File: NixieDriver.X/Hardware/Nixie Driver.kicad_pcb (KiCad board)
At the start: 4 copper layers, 21.1 x 31.8 mm, 20 parts, among them J1 Conn_02x03_Odd_Even, J2 Conn_01x03, J3 Conn_02x03_Odd_Even, Q0 MMBTA42LT1G, Q1 MMBTA42LT1G, Q10 MMBTA42LT1G, Q2 MMBTA42LT1G, Q3 MMBTA42LT1G, Q4 MMBTA42LT1G, Q5 MMBTA42LT1G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

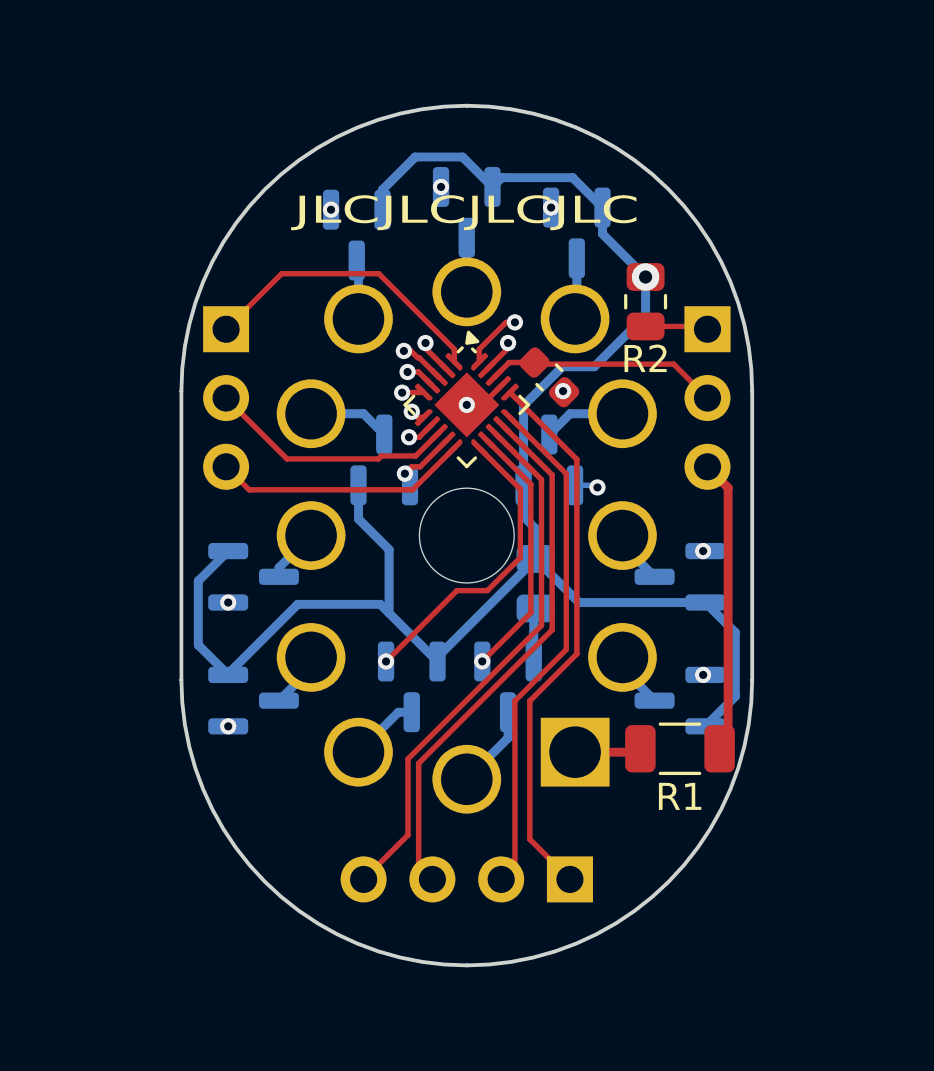
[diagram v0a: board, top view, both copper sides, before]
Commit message: Current-limiting-resistor for each driver
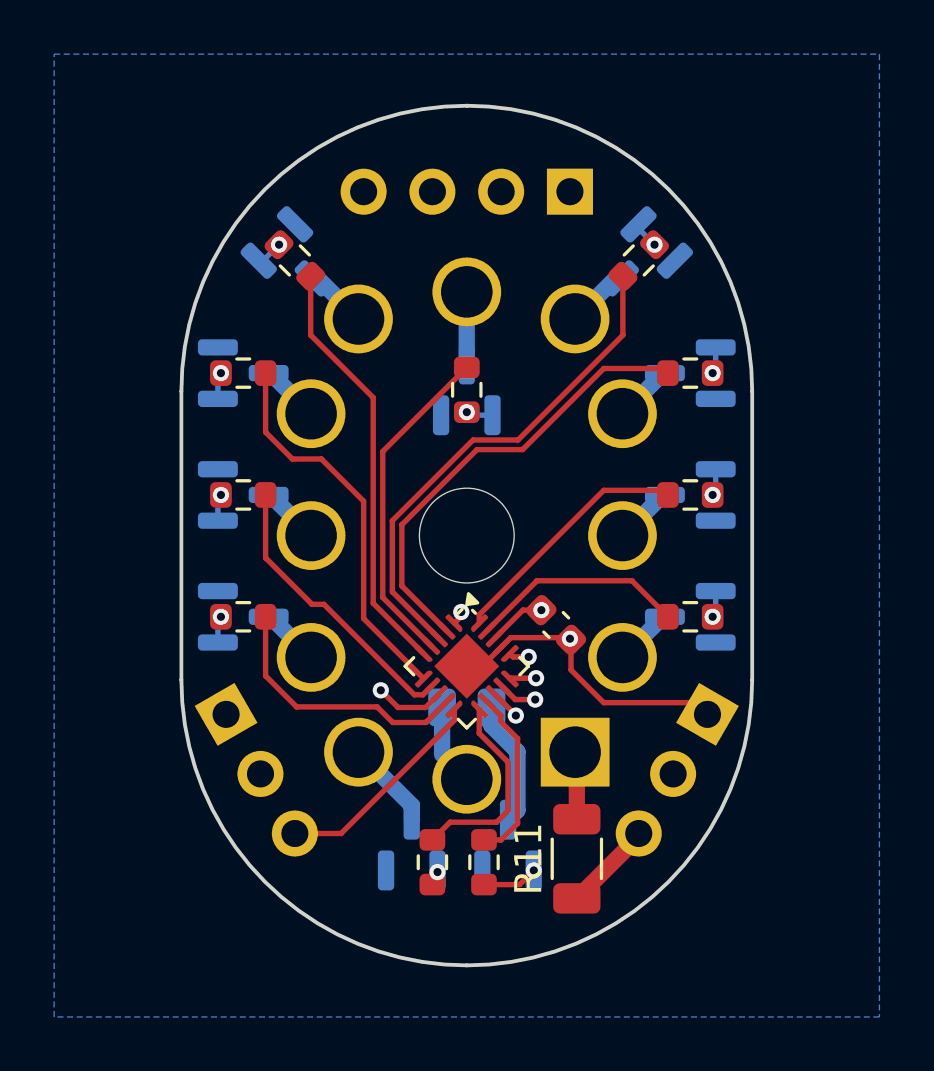
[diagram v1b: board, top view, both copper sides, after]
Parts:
- added R0: 2.2k, Resistor_SMD:R_0603_1608Metric, F.Cu at (160.7, 104.6)
- added R10: 2.2k, Resistor_SMD:R_0603_1608Metric, F.Cu at (153.0, 113.7)
- added R11: 20k, Resistor_SMD:R_1206_3216Metric, F.Cu at (156.5, 113.5)
- added R12: 150k, Resistor_SMD:R_0805_2012Metric, B.Cu at (152.4, 108.0)
- added R4: 2.2k, Resistor_SMD:R_0603_1608Metric, F.Cu at (144.1, 95.6)
- added R5: 2.2k, Resistor_SMD:R_0603_1608Metric, F.Cu at (146.1, 91.4)
- added R6: 2.2k, Resistor_SMD:R_0603_1608Metric, F.Cu at (152.4, 96.2)
- added R7: 2.2k, Resistor_SMD:R_0603_1608Metric, F.Cu at (158.8, 91.4)
- added R8: 2.2k, Resistor_SMD:R_0603_1608Metric, F.Cu at (160.7, 95.6)
- added R9: 2.2k, Resistor_SMD:R_0603_1608Metric, F.Cu at (160.7, 100.1)
- R1: value 20k -> 2.2k; footprint Resistor_SMD:R_1206_3216Metric -> Resistor_SMD:R_0603_1608Metric
- R2: footprint Resistor_SMD:R_0805_2012Metric -> Resistor_SMD:R_0603_1608Metric
- R3: value 0 -> 2.2k; footprint Resistor_SMD:R_0805_2012Metric -> Resistor_SMD:R_0603_1608Metric; moved to F.Cu
- moved J2 25.4 mm to (156.2, 88.9)
- moved R2 18.9 mm to (144.1, 104.6), turned to 180 degrees
- moved J1 14.2 mm to (143.5, 108.2), turned to -150 degrees
- moved J3 14.2 mm to (161.3, 108.2), turned to 150 degrees
- moved R3 11.3 mm to (144.1, 100.1), turned to 180 degrees
- moved R1 10.1 mm to (151.1, 113.7), turned to -90 degrees
- moved U1 9.65 mm to (152.4, 106.4)
- moved C1 9.15 mm to (155.7, 104.9)
- moved Q6 6.56 mm to (152.4, 96.2), turned to 90.029 degrees
- moved Q4 6.11 mm to (144.1, 95.6), turned to 0 degrees
- moved Q8 6.11 mm to (160.7, 95.6), turned to 180 degrees
- moved Q1 5.84 mm to (150.4, 113.0), turned to 90 degrees
- moved Q10 5.84 mm to (153.9, 113.0), turned to 90 degrees
- moved Q0 3.12 mm to (160.7, 104.6)
- moved Q2 3.12 mm to (144.1, 104.6)
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- renumbered C2 to C1, J3 to J2, J2 to J3
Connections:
- net /Cathode_0 renamed /Nixie Tube/Cathode 0/Cathode
- net /Cathode_1 renamed /Nixie Tube/Cathode 1/Cathode
- net /Cathode_2 renamed /Nixie Tube/Cathode 2/Cathode
- net /Cathode_3 renamed /Nixie Tube/Cathode 3/Cathode
- net /Cathode_4 renamed /Nixie Tube/Cathode 4/Cathode
- net /Cathode_5 renamed /Nixie Tube/Cathode 5/Cathode
- net /Cathode_6 renamed /Nixie Tube/Cathode 6/Cathode
- net /Cathode_7 renamed /Nixie Tube/Cathode 7/Cathode
- net /Cathode_8 renamed /Nixie Tube/Cathode 8/Cathode
- net /Cathode_9 renamed /Nixie Tube/Cathode 9/Cathode
- Q0 pad 1: /Driver_0 -> Net-(Q0-B)
- Q0 pad 2: N_GND -> GND
- Q1 pad 1: /Driver_1 -> Net-(Q1-B)
- Q1 pad 2: N_GND -> GND
- Q10 pad 1: /Driver_Dot -> Net-(Q10-B)
- Q10 pad 2: Net-(Q10-E) -> GND
- Q10 pad 3: /Cathode_Dot -> /Nixie Tube/Cathode Dot/Cathode
- Q2 pad 1: /Driver_2 -> Net-(Q2-B)
- Q2 pad 2: N_GND -> GND
- Q3 pad 1: /Driver_3 -> Net-(Q3-B)
- Q3 pad 2: N_GND -> GND
- Q4 pad 1: /Driver_4 -> Net-(Q4-B)
- Q4 pad 2: N_GND -> GND
- Q5 pad 1: /Driver_5 -> Net-(Q5-B)
- Q5 pad 2: N_GND -> GND
- Q6 pad 1: /Driver_6 -> Net-(Q6-B)
- Q6 pad 2: N_GND -> GND
- Q7 pad 1: /Driver_7 -> Net-(Q7-B)
- Q7 pad 2: N_GND -> GND
- Q8 pad 1: /Driver_8 -> Net-(Q8-B)
- Q8 pad 2: N_GND -> GND
- Q9 pad 1: /Driver_9 -> Net-(Q9-B)
- Q9 pad 2: N_GND -> GND
- R1 pad 1: Net-(V1-V+) -> /Driver_1
- R1 pad 2: Vnn -> Net-(Q1-B)
- R2 pad 1: N_GND -> /Driver_2
- R2 pad 2: GND -> Net-(Q2-B)
- R3 pad 1: Net-(Q10-E) -> /Driver_3
- R3 pad 2: N_GND -> Net-(Q3-B)
- U1 pad 2: /Driver_7 -> /Driver_8
- U1 pad 3: /Driver_6 -> /Driver_7
- U1 pad 4: /Driver_5 -> /Driver_6
- U1 pad 5: /Driver_8 -> /Driver_5
- U1 pad 6: /Driver_3 -> /Driver_4
- U1 pad 7: /Driver_2 -> /Driver_3
- U1 pad 9: /Driver_4 -> /Driver_2
- V1 pad 12: /Cathode_Dot -> Net-(V1-DP)
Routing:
- net N_GND: track 65.1 -> 0.00 mm, vias 1 -> 0
- net /Driver_4: track 2.56 -> 14.3 mm, vias 1 -> 0
- net /Driver_0: track 17.0 -> 8.00 mm, vias 2 -> 0
- net /Driver_7: track 9.77 -> 18.6 mm, vias 2 -> 0
- net Vnn: track 10.8 -> 3.34 mm
- net GND: track 4.01 -> 11.2 mm, vias 2 -> 1
- net /Driver_8: track 10.3 -> 16.9 mm, vias 2 -> 0
- net /Driver_5: track 10.1 -> 15.7 mm, vias 2 -> 0
- net /Driver_2: track 14.9 -> 9.90 mm, vias 2 -> 0
- net /Driver_9: track 14.0 -> 9.25 mm, vias 2 -> 0
- net /Nixie Tube/Cathode Dot/Cathode: track 0.00 -> 4.68 mm
- net /ADDR3: track 19.9 -> 24.3 mm, vias 0 -> 1
- net /Driver_6: track 8.32 -> 12.3 mm, vias 2 -> 0
- net /ADDR1/CLK: track 18.9 -> 22.8 mm, vias 0 -> 1
- net /Driver_1: track 11.2 -> 7.43 mm, vias 1 -> 0
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- added copper zone on B.Cu, net GND
- removed copper zone on In1.Cu, net GND
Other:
- board text removed: "JLCJLCJLCJLC"

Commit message: Small layout tweaks.
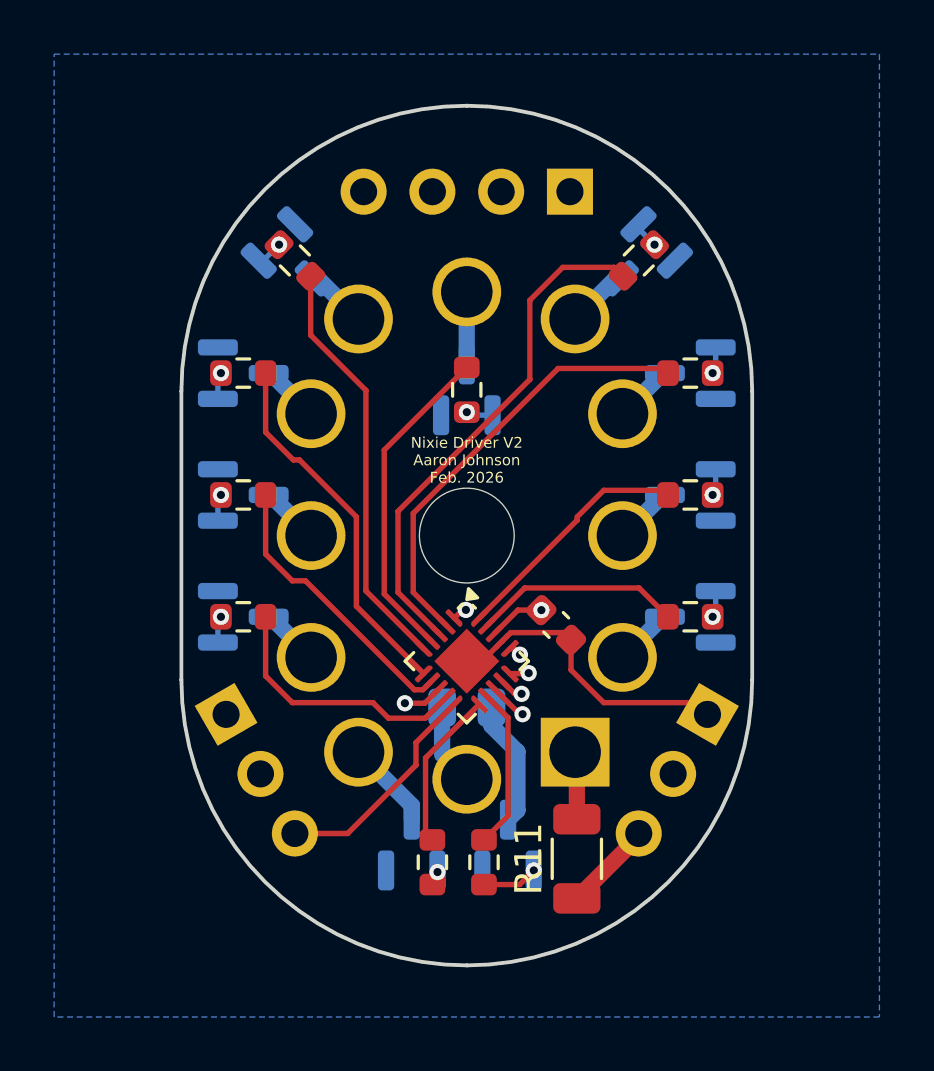
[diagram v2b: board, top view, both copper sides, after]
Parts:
- moved U1 0.19 mm to (152.4, 106.2)
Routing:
- net /ADDR1/CLK: track 22.8 -> 19.9 mm
- net /ADDR2: track 23.2 -> 21.5 mm
- net /Driver_1: track 7.43 -> 5.94 mm
- net /ADDR3: track 24.3 -> 23.4 mm
- net /Driver_4: track 14.3 -> 13.6 mm
- net /~{MCLR}: track 11.5 -> 11.0 mm
- net /Driver_8: track 16.9 -> 16.4 mm
- net GND: vias 1 -> 0
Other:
- board text added: "Nixie Driver V2 Aaron Johnson Feb. 2026"
